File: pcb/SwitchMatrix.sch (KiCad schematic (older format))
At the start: 56 parts, among them K00 KEYSW, K01 KEYSW, K02 KEYSW, K03 KEYSW, K04 KEYSW, K05 KEYSW, K10 KEYSW, K11 KEYSW, K12 KEYSW, K13 KEYSW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

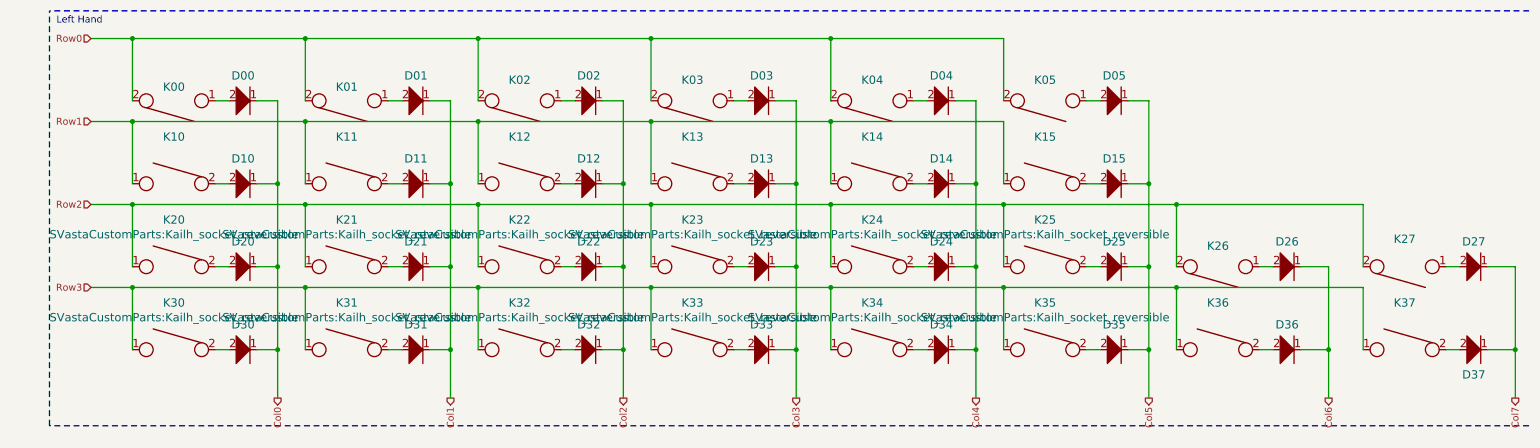
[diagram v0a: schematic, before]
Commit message: Removed most keys to prepare for test PCB
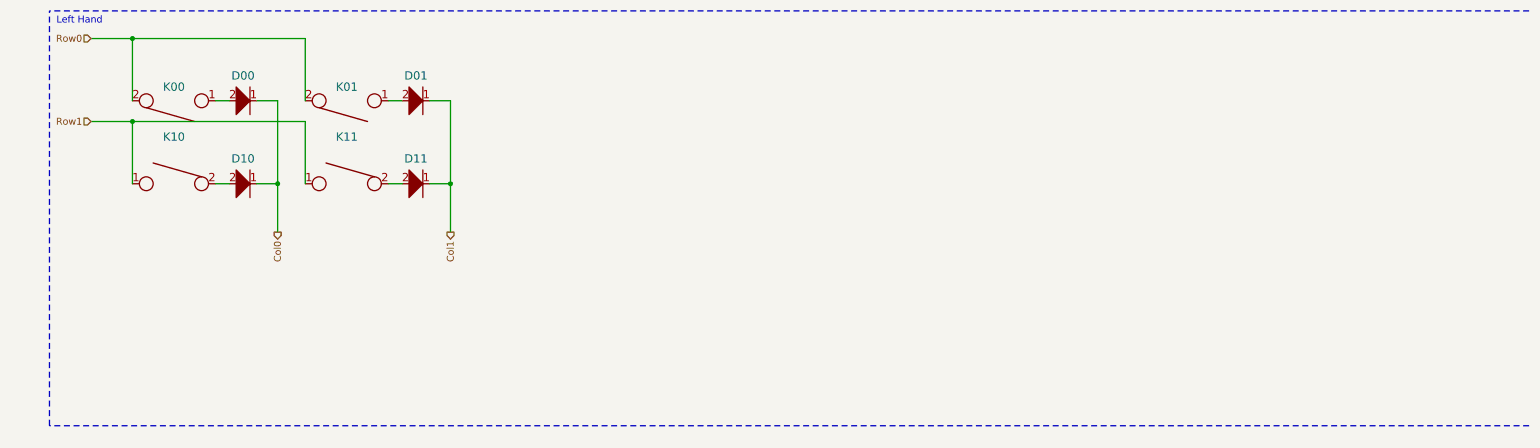
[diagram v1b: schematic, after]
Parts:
- removed D02, D03, D04, D05, D12, D13, D14, D15, D20, D21, D22, D23, D24, D25, D26, D27, D30, D31, D32, D33, D34, D35, D36, D37: D, SVastaCustomParts:D_MiniMELF_Handsoldering_Shorter_Pads_DoubleSided, symbol Keeb-rescue:D-Keyboard_Parts-Keeb-rescue
- removed K02, K03, K04, K05, K12, K13, K14, K15, K20, K21, K22, K23, K24, K25, K26, K27, K30, K31, K32, K33, K34, K35, K36, K37: KEYSW, SVastaCustomParts:Kailh_socket_reversible, symbol Keeb-rescue:KEYSW-Keyboard_Parts-Keeb-rescue
